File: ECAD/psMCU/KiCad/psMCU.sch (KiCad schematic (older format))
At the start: 0 parts

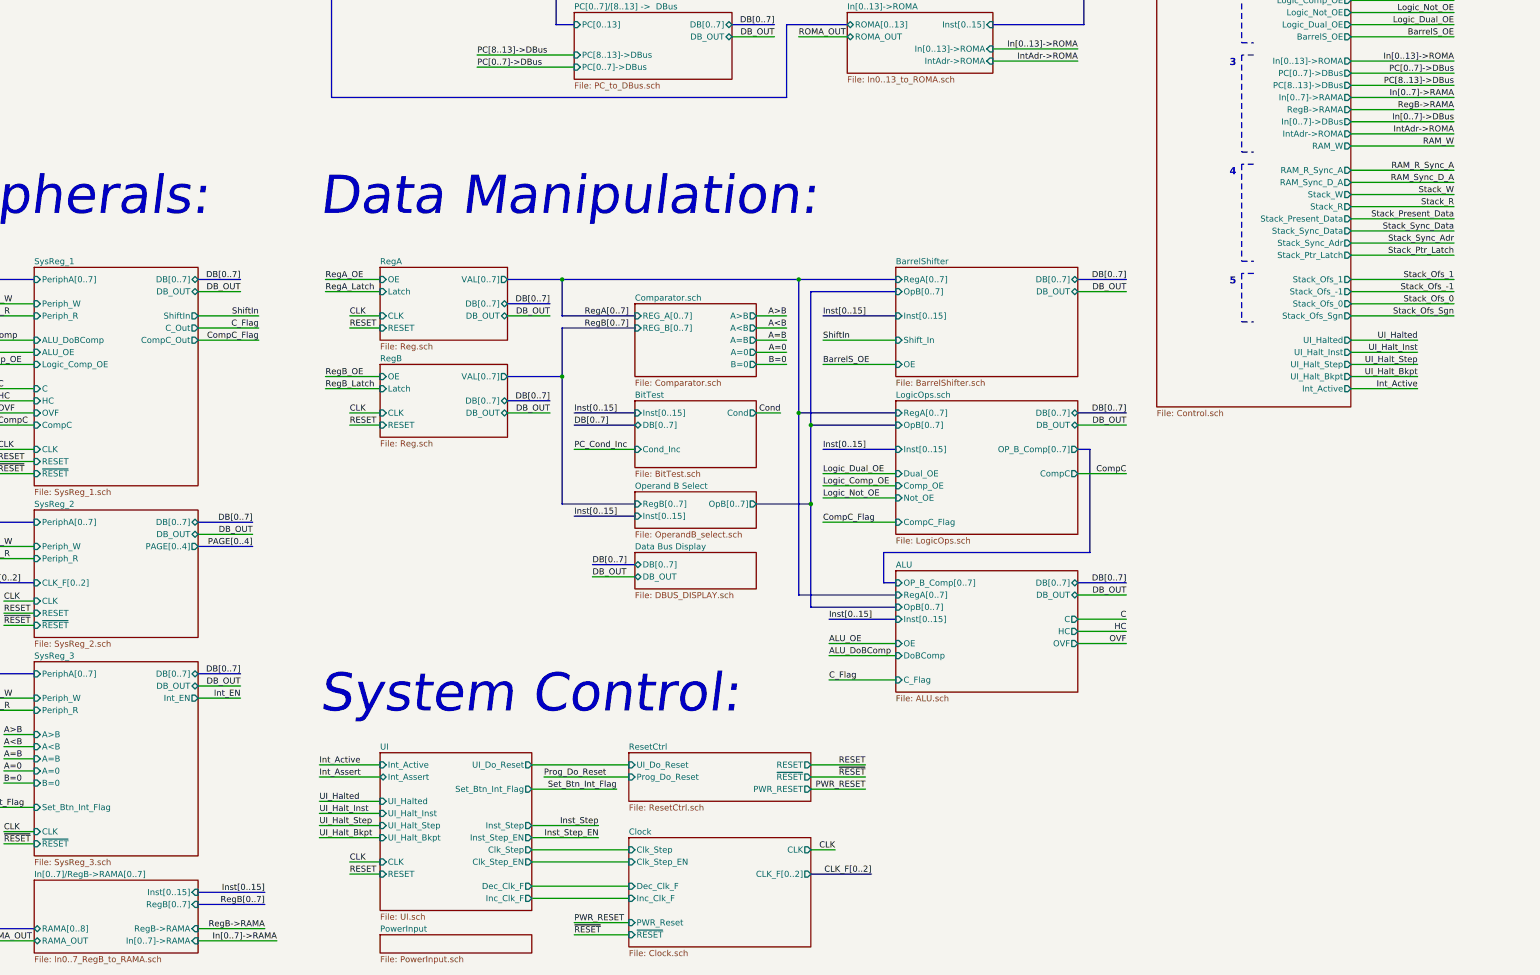
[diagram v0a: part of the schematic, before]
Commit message: Sch: Changed LDD behaviour (now is literal+b)
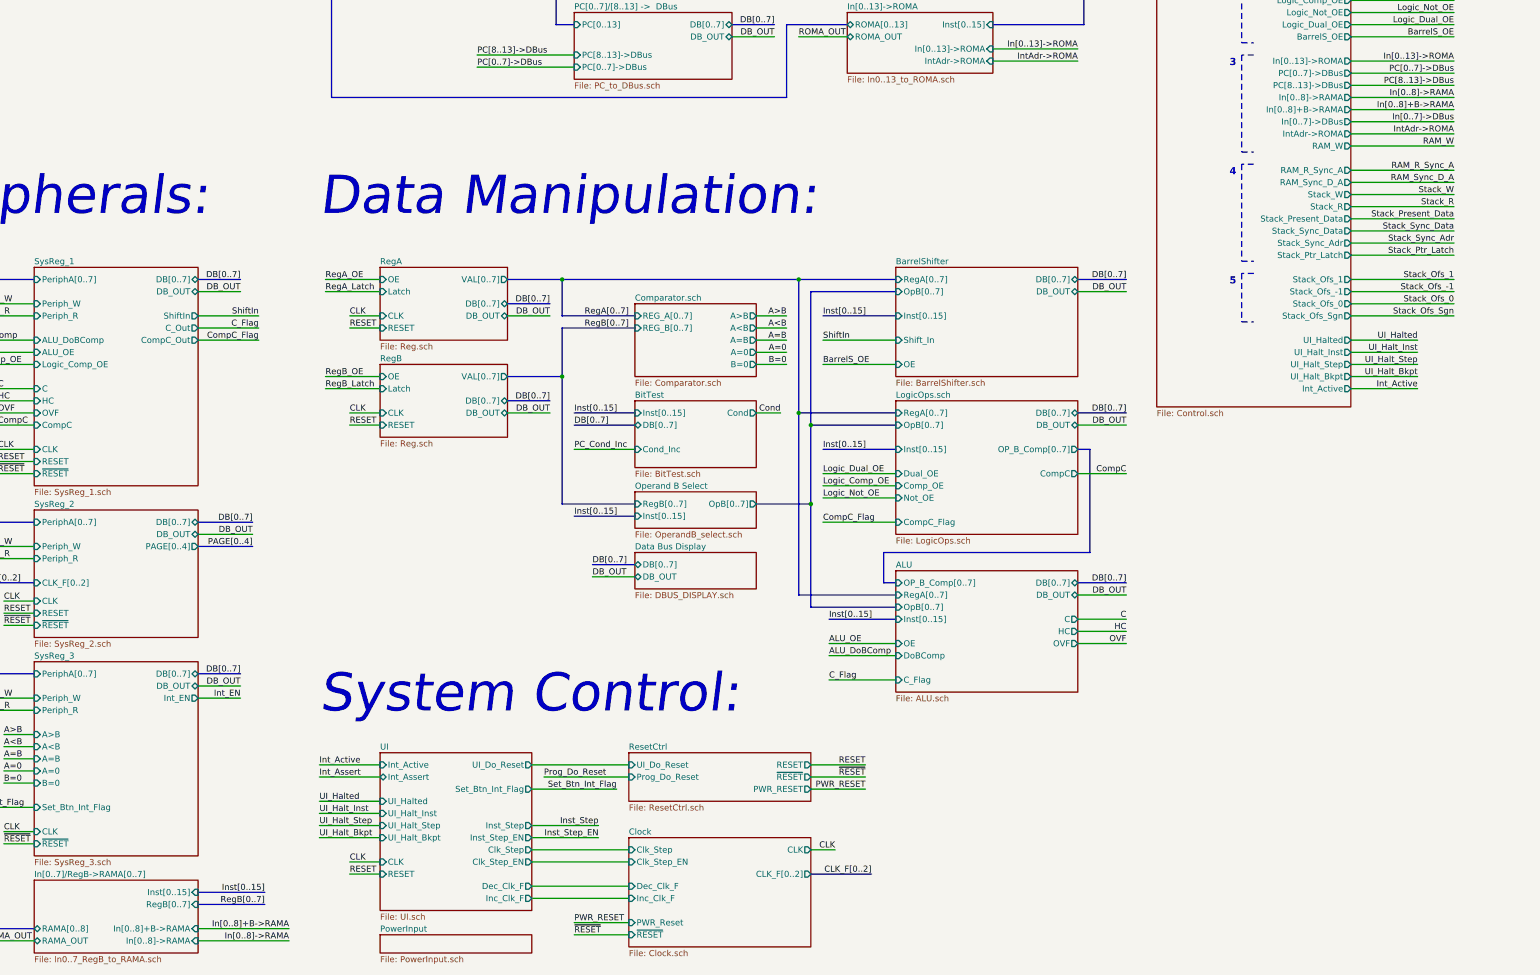
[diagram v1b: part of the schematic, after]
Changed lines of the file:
@@
 Wire Wire Line
 	15000 1400 15850 1400
-Text Label 15850 3900 2    50   ~ 0
-RegB->RAMA
-Text Label 15850 3800 2    50   ~ 0
-In[0..7]->RAMA
-Wire Wire Line
-	15000 3900 15850 3900
-Wire Wire Line
-	15000 3800 15850 3800
 Wire Wire Line
 	4150 1700 4800 1700
@@
 F49 "IntAdr->ROMA" O R 15000 4100 50
 F50 "Stack_Ofs_Sgn" O R 15000 5600 50
-F51 "In[0..7]->RAMA" O R 15000 3800 50
-F52 "RegB->RAMA" O R 15000 3900 50
+F51 "In[0..8]->RAMA" O R 15000 3800 50
+F52 "In[0..8]+B->RAMA" O R 15000 3900 50
 $EndSheet
 Wire Notes Line
@@
 F4 "RAMA[0..8]" B L 4150 10650 50
 F5 "RAMA_OUT" T L 4150 10750 50
-F6 "RegB->RAMA" I R 5500 10650 50
-F7 "In[0..7]->RAMA" I R 5500 10750 50
+F6 "In[0..8]+B->RAMA" I R 5500 10650 50
+F7 "In[0..8]->RAMA" I R 5500 10750 50
 $EndSheet
 Wire Wire Line
@@
 Text Label 3900 8150 0    50   ~ 0
 ~RESET
-$Sheet
-S 4150 5200 1350 1800
-U 5FD65262
-F0 "SysReg_1" 50
-F1 "SysReg_1.sch" 50
-F2 "PeriphA[0..7]" I L 4150 5300 50
-F3 "Periph_W" I L 4150 5500 50
-F4 "Periph_R" I L 4150 5600 50
-F5 "~RESET" I L 4150 6900 50
-F6 "DB_OUT" T R 5500 5400 50
-F7 "DB[0..7]" T R 5500 5300 50
-F8 "ShiftIn" O R 5500 5600 50
-F9 "C_Out" O R 5500 5700 50
-F10 "CompC_Out" O R 5500 5800 50
-F11 "CLK" I L 4150 6700 50
-F12 "RESET" I L 4150 6800 50
-F13 "C" I L 4150 6200 50
-F14 "HC" I L 4150 6300 50
-F15 "CompC" I L 4150 6500 50
-F16 "OVF" I L 4150 6400 50
-F17 "ALU_DoBComp" I L 4150 5800 50
-F18 "ALU_OE" I L 4150 5900 50
-F19 "Logic_Comp_OE" I L 4150 6000 50
-$EndSheet
 Wire Wire Line
 	3850 6700 4150 6700
@@
 Wire Bus Line
 	8500 6100 8500 7150
-Text Label 6050 10650 2    50   ~ 0
-RegB->RAMA
-Text Label 6150 10750 2    50   ~ 0
-In[0..7]->RAMA
-Wire Wire Line
-	5500 10650 6050 10650
-Wire Wire Line
-	5500 10750 6150 10750
+Text Label 6250 10650 2    50   ~ 0
+In[0..8]+B->RAMA
+Text Label 6250 10750 2    50   ~ 0
+In[0..8]->RAMA
+Wire Wire Line
+	5500 10650 6250 10650
+Wire Wire Line
+	5500 10750 6250 10750
 Text Label 10350 2600 2    50   ~ 0
 PWR_RESET
@@
 Wire Bus Line
 	10350 3200 10850 3200
+$Sheet
+S 4150 5200 1350 1800
+U 5FD65262
+F0 "SysReg_1" 50
+F1 "SysReg_1.sch" 50
+F2 "PeriphA[0..7]" I L 4150 5300 50
+F3 "Periph_W" I L 4150 5500 50
+F4 "Periph_R" I L 4150 5600 50
+F5 "~RESET" I L 4150 6900 50
+F6 "DB_OUT" T R 5500 5400 50
+F7 "DB[0..7]" T R 5500 5300 50
+F8 "ShiftIn" O R 5500 5600 50
+F9 "C_Out" O R 5500 5700 50
+F10 "CompC_Out" O R 5500 5800 50
+F11 "CLK" I L 4150 6700 50
+F12 "RESET" I L 4150 6800 50
+F13 "C" I L 4150 6200 50
+F14 "HC" I L 4150 6300 50
+F15 "CompC" I L 4150 6500 50
+F16 "OVF" I L 4150 6400 50
+F17 "ALU_DoBComp" I L 4150 5800 50
+F18 "ALU_OE" I L 4150 5900 50
+F19 "Logic_Comp_OE" I L 4150 6000 50
+$EndSheet
+Text Label 15850 3900 2    50   ~ 0
+In[0..8]+B->RAMA
+Text Label 15850 3800 2    50   ~ 0
+In[0..8]->RAMA
+Wire Wire Line
+	15000 3800 15850 3800
+Wire Wire Line
+	15000 3900 15850 3900
 $EndSCHEMATC

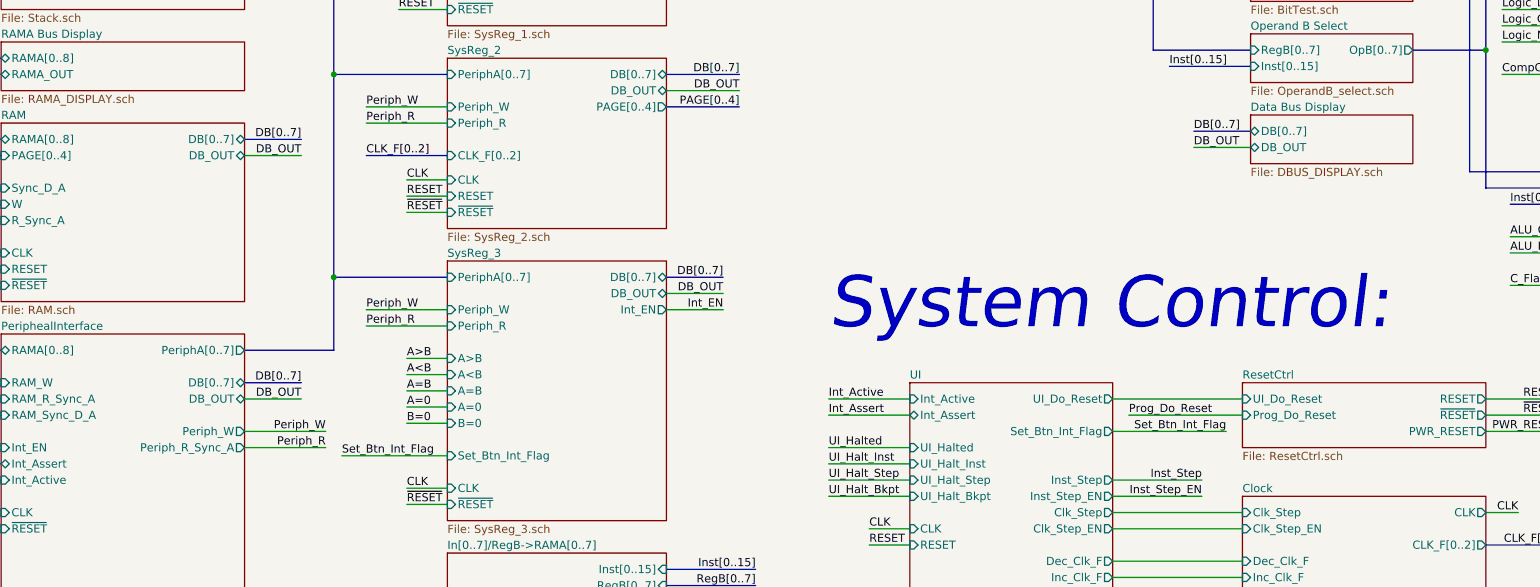
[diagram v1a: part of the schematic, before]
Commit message: Sch: Reworked Peripheral Interface (Buffers)
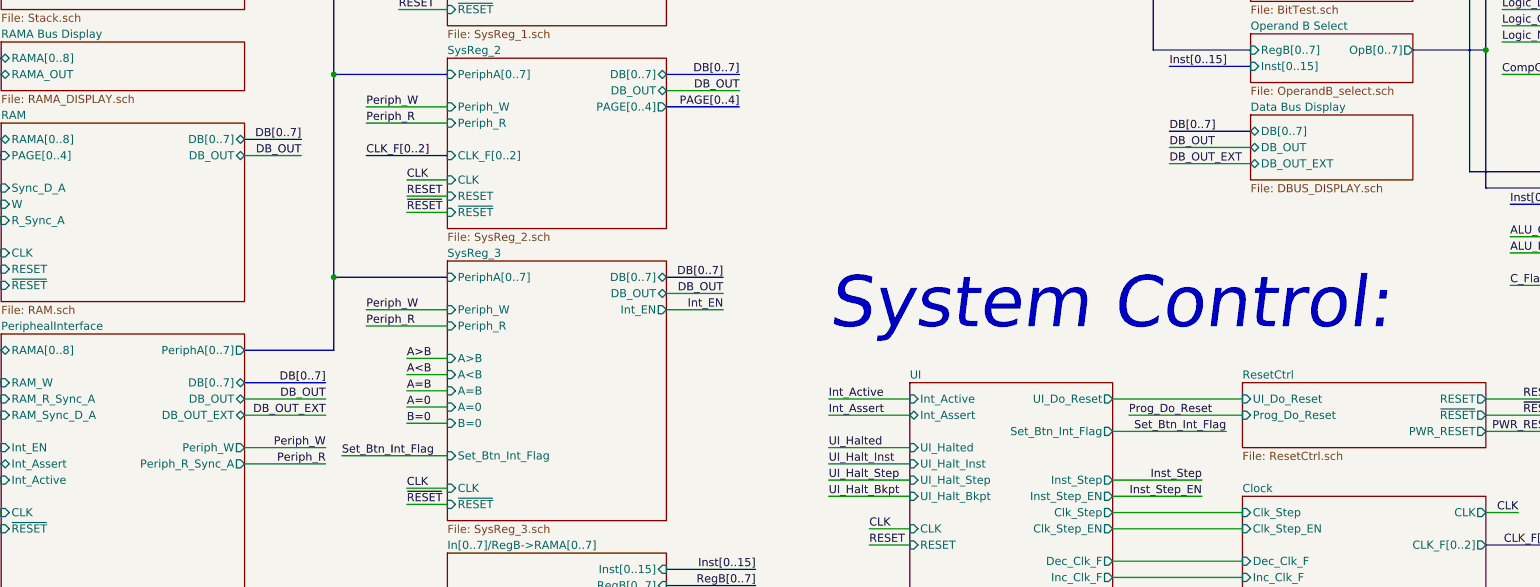
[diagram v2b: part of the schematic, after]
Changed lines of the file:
@@
 $Descr A3 16535 11693
 encoding utf-8
-Sheet 1 97
+Sheet 1 96
 Title "psMCU"
 Date "2022-02-13"
@@
 Wire Wire Line
 	1000 7300 1400 7300
-Text Label 3250 9200 2    50   ~ 0
+Text Label 3400 9200 2    50   ~ 0
 DB[0..7]
 Wire Bus Line
-	2900 9200 3250 9200
-Text Label 3250 9300 2    50   ~ 0
+	2900 9200 3400 9200
+Text Label 3400 9300 2    50   ~ 0
 DB_OUT
 Wire Wire Line
-	2900 9300 3250 9300
+	2900 9300 3400 9300
 Wire Wire Line
 	1400 9700 950  9700
@@
 F8 "RAM_W" I L 1400 9200 50
 F9 "RAM_R_Sync_A" I L 1400 9300 50
-F10 "Periph_W" O R 2900 9500 50
+F10 "Periph_W" O R 2900 9600 50
 F11 "PeriphA[0..7]" O R 2900 9000 50
 F12 "Int_Active" I L 1400 9800 50
 F13 "Int_Assert" B L 1400 9700 50
 F14 "Int_EN" I L 1400 9600 50
-F15 "Periph_R_Sync_A" O R 2900 9600 50
+F15 "Periph_R_Sync_A" O R 2900 9700 50
+F16 "DB_OUT_EXT" T R 2900 9400 50
 $EndSheet
 Wire Wire Line
@@
 Wire Wire Line
 	950  9600 1400 9600
-Text Label 3400 9500 2    50   ~ 0
+Text Label 3400 9600 2    50   ~ 0
 Periph_W
-Text Label 3400 9600 2    50   ~ 0
+Text Label 3400 9700 2    50   ~ 0
 Periph_R
 Wire Wire Line
-	3400 9500 2900 9500
-Wire Wire Line
-	2900 9600 3400 9600
+	3400 9600 2900 9600
+Wire Wire Line
+	2900 9700 3400 9700
 Text Label 3650 5500 0    50   ~ 0
 Periph_W
@@
 $EndSheet
 $Sheet
-S 9100 7550 1000 300
+S 9100 7550 1000 400
 U 5F394B96
 F0 "Data Bus Display" 50
@@
 F2 "DB_OUT" T L 9100 7750 50
 F3 "DB[0..7]" T L 9100 7650 50
+F4 "DB_OUT_EXT" T L 9100 7850 50
 $EndSheet
 $Sheet
@@
 	12750 6700 12850 6700
 Wire Wire Line
-	9100 7750 8750 7750
-Text Label 8750 7750 0    50   ~ 0
+	9100 7750 8600 7750
+Text Label 8600 7750 0    50   ~ 0
 DB_OUT
 Text Label 9050 5600 2    50   ~ 0
 RegA[0..7]
 Wire Bus Line
-	9100 7650 8750 7650
-Text Label 8750 7650 0    50   ~ 0
+	9100 7650 8600 7650
+Text Label 8600 7650 0    50   ~ 0
 DB[0..7]
 Wire Bus Line
@@
 Wire Wire Line
 	15000 3900 15850 3900
+Wire Wire Line
+	3400 9400 2900 9400
+Text Label 3400 9400 2    50   ~ 0
+DB_OUT_EXT
+Text Label 8600 7850 0    50   ~ 0
+DB_OUT_EXT
+Wire Wire Line
+	8600 7850 9100 7850
 $EndSCHEMATC
